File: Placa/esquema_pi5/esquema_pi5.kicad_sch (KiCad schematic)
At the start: 24 parts, among them J2 Screw_Terminal_01x02, Q1 BC547, Q2 BC547, U2 AMS1117-3.3, U3 LM7805_TO220

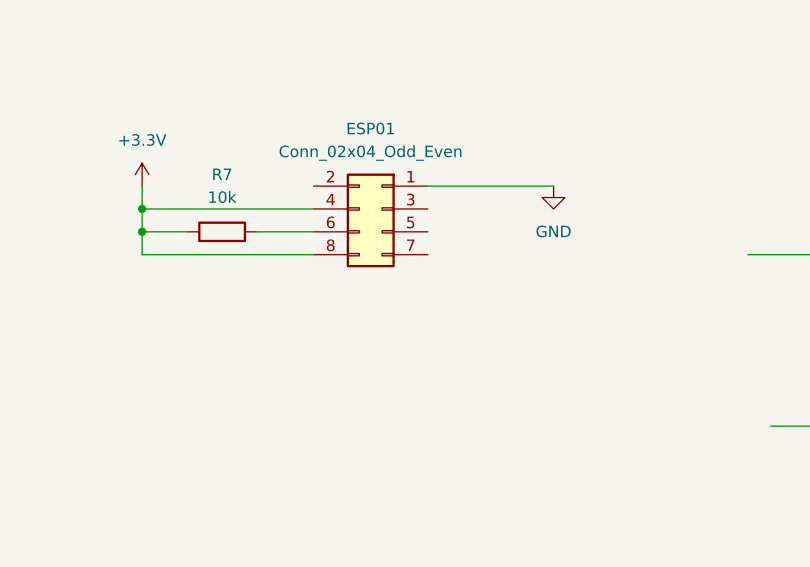
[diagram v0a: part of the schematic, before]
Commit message: Add botão reset esquema da placa
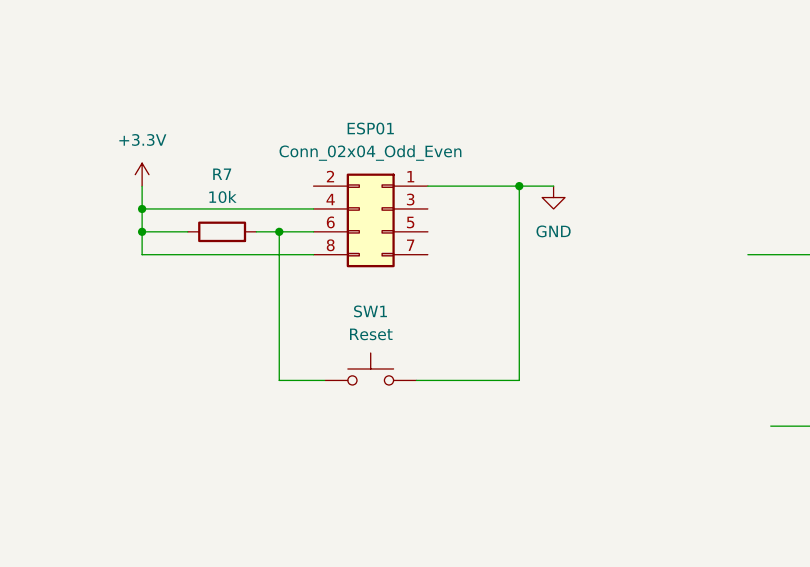
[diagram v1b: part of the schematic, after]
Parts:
- added SW1: Reset, symbol Switch:SW_Push
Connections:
- net GND: now also SW1.2
- net at ESP01.6 (Pin_6), R7.2: now also SW1.1
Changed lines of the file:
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@@
+	)
+	(junction
+		(at 151.13 110.49)
+		(diameter 0)
+		(color 0 0 0 0)
 	)
 	(junction
@@
 	)
 	(junction
+		(at 124.46 115.57)
+		(diameter 0)
+		(color 0 0 0 0)
+	)
+	(junction
 		(at 200.66 48.26)
 		(diameter 0)
@@
 	(wire
 		(pts
+			(xy 129.54 132.08) (xy 124.46 132.08)
+		)
+		(stroke
+			(width 0)
+			(type default)
+		)
+	)
+	(wire
+		(pts
 			(xy 214.63 113.03) (xy 214.63 109.22)
 		)
@@
 	(wire
 		(pts
-			(xy 140.97 110.49) (xy 154.94 110.49)
-		)
-		(stroke
-			(width 0)
-			(type default)
-		)
-	)
-	(wire
-		(pts
 			(xy 217.17 109.22) (xy 217.17 102.87)
 		)
@@
 	(wire
 		(pts
+			(xy 151.13 132.08) (xy 151.13 110.49)
+		)
+		(stroke
+			(width 0)
+			(type default)
+		)
+	)
+	(wire
+		(pts
 			(xy 125.73 59.69) (xy 140.97 59.69)
 		)
@@
 	(wire
 		(pts
+			(xy 124.46 115.57) (xy 128.27 115.57)
+		)
+		(stroke
+			(width 0)
+			(type default)
+		)
+	)
+	(wire
+		(pts
 			(xy 110.49 49.53) (xy 110.49 52.07)
 		)
@@
 	(wire
 		(pts
+			(xy 151.13 110.49) (xy 154.94 110.49)
+		)
+		(stroke
+			(width 0)
+			(type default)
+		)
+	)
+	(wire
+		(pts
 			(xy 140.97 44.45) (xy 140.97 49.53)
 		)
@@
 	(wire
 		(pts
+			(xy 124.46 132.08) (xy 124.46 115.57)
+		)
+		(stroke
+			(width 0)
+			(type default)
+		)
+	)
+	(wire
+		(pts
+			(xy 140.97 110.49) (xy 151.13 110.49)
+		)
+		(stroke
+			(width 0)
+			(type default)
+		)
+	)
+	(wire
+		(pts
 			(xy 55.88 107.95) (xy 58.42 107.95)
 		)
@@
 	(wire
 		(pts
-			(xy 121.92 115.57) (xy 128.27 115.57)
+			(xy 139.7 132.08) (xy 151.13 132.08)
+		)
+		(stroke
+			(width 0)
+			(type default)
+		)
+	)
+	(wire
+		(pts
+			(xy 121.92 115.57) (xy 124.46 115.57)
 		)
 		(stroke
@@
 					(unit 1)
 				)
+			)
+		)
+	)
+	(symbol
+		(lib_id "Switch:SW_Push")
+		(at 134.62 132.08 0)
+		(unit 1)
+		(exclude_from_sim no)
+		(in_bom yes)
+		(on_board yes)
+		(dnp no)
+		(fields_autoplaced yes)
+		(property "Reference" "SW1"
+			(at 134.62 124.46 0)
+			(effects
+				(font
+					(size 1.27 1.27)
+				)
+			)
+		)
+		(property "Value" "Reset"
+			(at 134.62 127 0)
+			(effects
+				(font
+					(size 1.27 1.27)
+				)
+			)
+		)
+		(property "Footprint" ""
+			(at 134.62 127 0)
+			(effects
+				(font
+					(size 1.27 1.27)
+				)
+				(hide yes)
+			)
+		)
+		(property "Datasheet" "~"
+			(at 134.62 127 0)
+			(effects
+				(font
+					(size 1.27 1.27)
+				)
+				(hide yes)
+			)
+		)
+		(property "Description" "Push button switch, generic, two pins"
+			(at 134.62 132.08 0)
+			(effects
+				(font
+					(size 1.27 1.27)
+				)
+				(hide yes)
+			)
+		)
+		(pin "2"
+		)
+		(pin "1"
+		)
+		(instances
+			(project ""
+				(path "/20b03a6f-999d-484b-9a62-fce4f78eaac1"
+					(reference "SW1")
+					(unit 1)
+				)
